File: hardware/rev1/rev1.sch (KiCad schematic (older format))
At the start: 37 parts, among them J1 Conn_01x09_Female, J2 RFM9X_header, J3 Conn_01x03_Male, U1 BNO055, U2 MPL3115A2, U3 Teensy3.6, U4 BMI088, U5 ADXL345BCCZ, Y1 Crystal_32kHz768

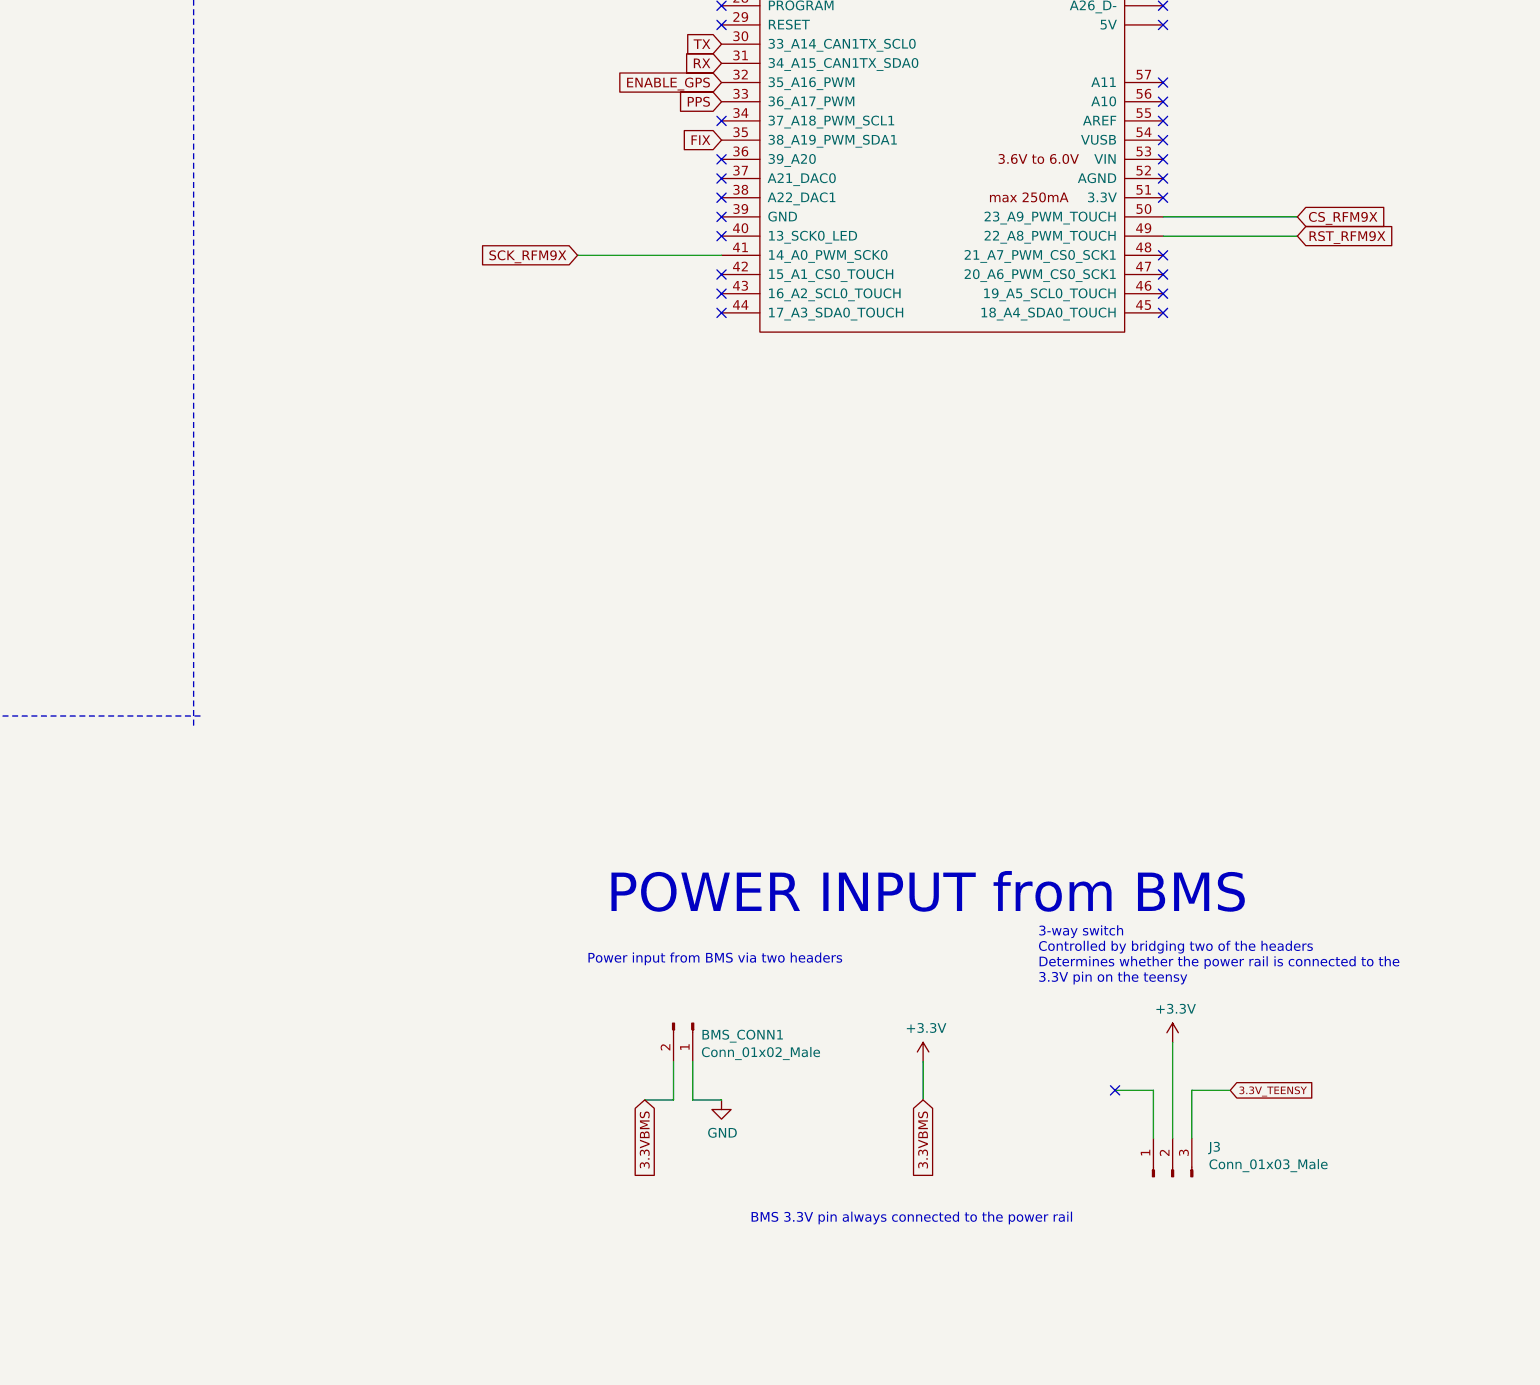
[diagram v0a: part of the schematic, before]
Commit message: add diode between Vin on Teensy and VDD on BMS
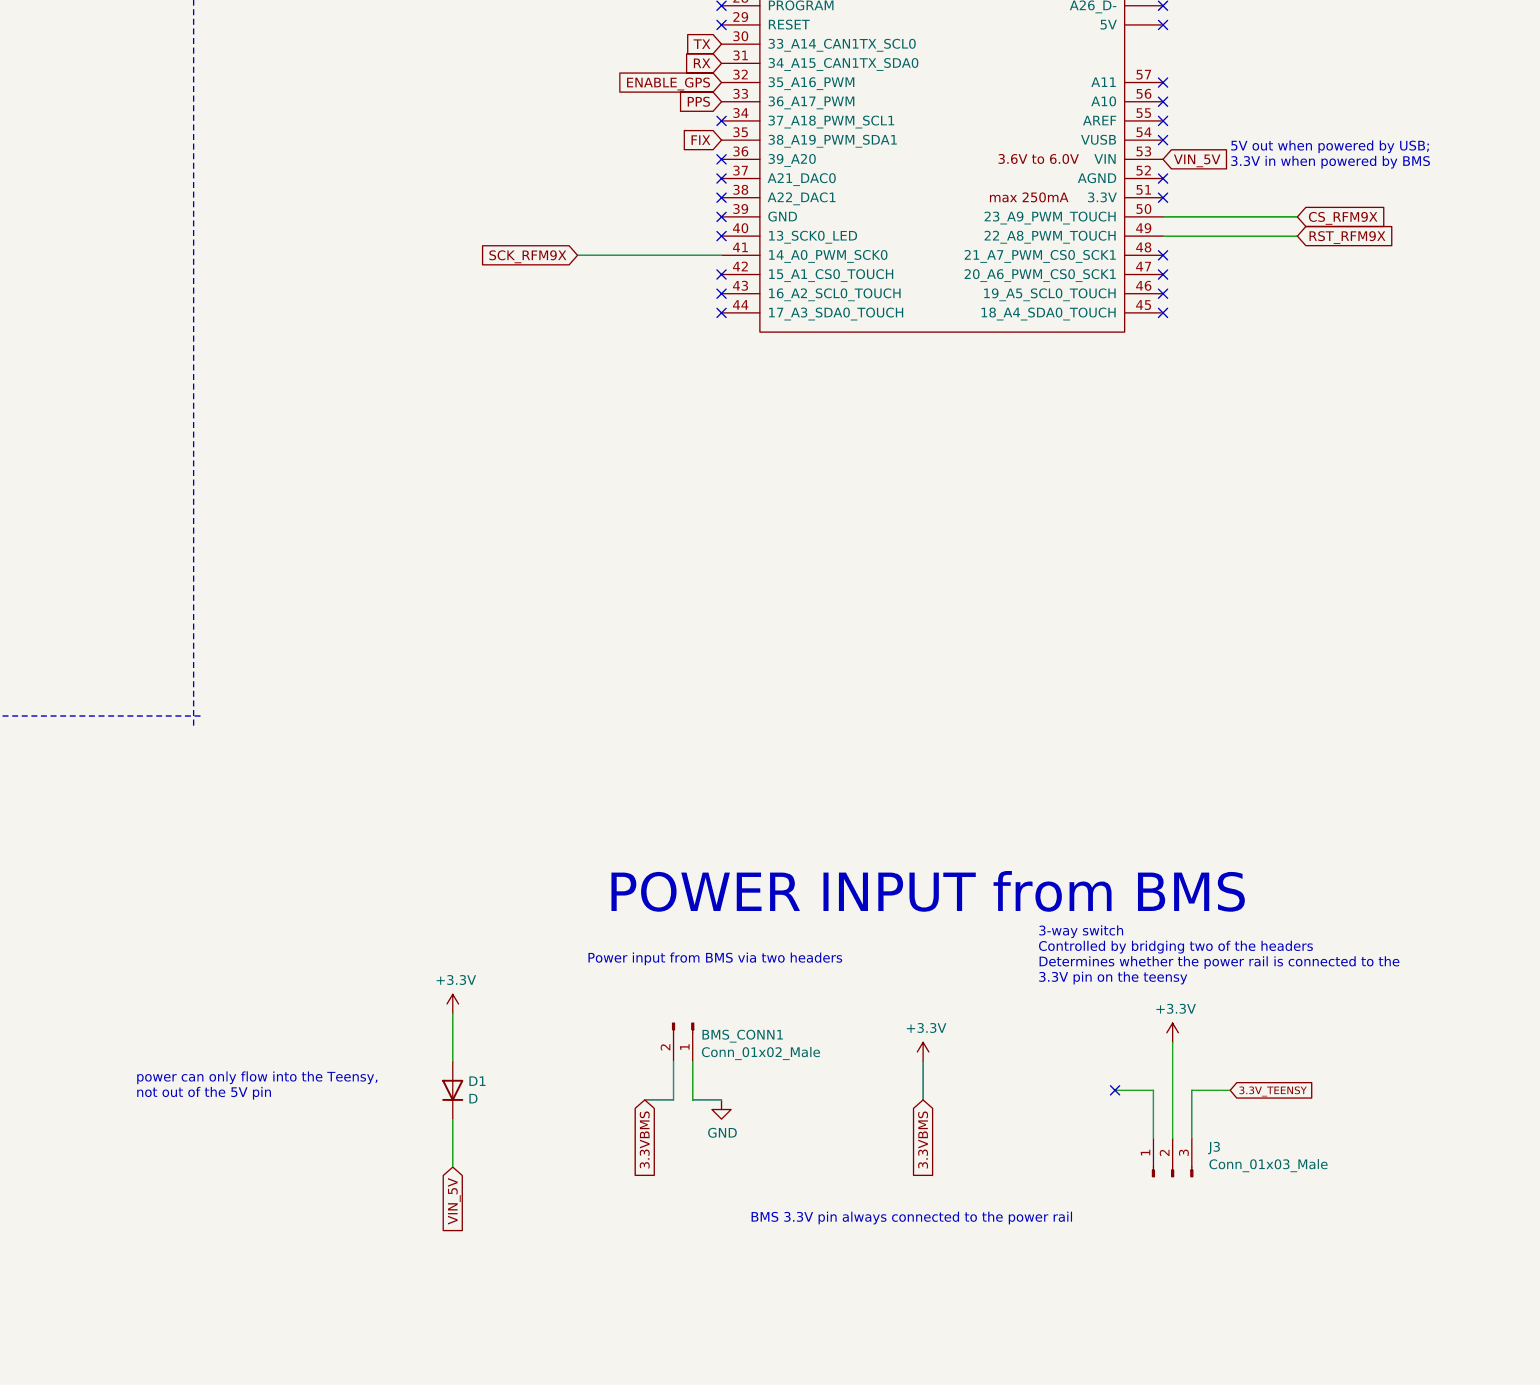
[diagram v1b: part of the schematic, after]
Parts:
- added D1: D, footprints:D_0805_OEM, symbol Device:D
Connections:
- net +3V3: now also D1.2 (A)
- net VIN_5V: now reaches U3.53 (VIN)
- net VIN_5V: now also D1.1 (K)
- no-connect marks 67 -> 66
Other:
- note added: "5V out when powered by USB;\n3.3V in when powered by BMS"
- note added: "power can only flow into the Teensy,\nnot out of the 5V pin"
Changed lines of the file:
@@
 Wire Wire Line
 	27250 11200 27400 11200
-NoConn ~ 29700 6300
 NoConn ~ 27400 4300
 NoConn ~ 27400 4400
@@
 NoConn ~ 29450 11150
 $Comp
-L power:GND #PWR?
+L power:GND #PWR04
 U 1 1 60246ABA
 P 27400 11200
-F 0 "#PWR?" H 27400 10950 50  0001 C CNN
+F 0 "#PWR04" H 27400 10950 50  0001 C CNN
 F 1 "GND" H 27405 11027 50  0000 C CNN
 F 2 "" H 27400 11200 50  0001 C CNN
@@
 	1    0    0    -1
 $EndComp
+Text GLabel 29700 6300 2    50   Input ~ 0
+VIN_5V
+Text Notes 30050 6350 0    50   ~ 0
+5V out when powered by USB;\n3.3V in when powered by BMS
+Text GLabel 26000 11550 3    50   Input ~ 0
+VIN_5V
+$Comp
+L power:+3.3V #PWR03
+U 1 1 6027438B
+P 26000 10750
+F 0 "#PWR03" H 26000 10600 50  0001 C CNN
+F 1 "+3.3V" H 26015 10923 50  0000 C CNN
+F 2 "" H 26000 10750 50  0001 C CNN
+F 3 "" H 26000 10750 50  0001 C CNN
+	1    26000 10750
+	1    0    0    -1
+$EndComp
+$Comp
+L Device:D D1
+U 1 1 60275618
+P 26000 11150
+F 0 "D1" V 26046 11070 50  0000 R CNN
+F 1 "D" V 25955 11070 50  0000 R CNN
+F 2 "footprints:D_0805_OEM" H 26000 11150 50  0001 C CNN
+F 3 "~" H 26000 11150 50  0001 C CNN
+	1    26000 11150
+	0    -1   -1   0
+$EndComp
+Wire Wire Line
+	26000 10750 26000 11000
+Wire Wire Line
+	26000 11300 26000 11550
+Text Notes 24350 11200 0    50   ~ 0
+power can only flow into the Teensy,\nnot out of the 5V pin
 $EndSCHEMATC

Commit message: move GPS pins away from Teensy
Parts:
- J3: footprint Connector_PinSocket_2.54mm:PinSocket_1x03_P2.54mm_Vertical -> Connector_PinHeader_2.54mm:PinHeader_1x03_P2.54mm_Vertical
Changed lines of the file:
@@
 F 0 "J3" V 29904 11412 50  0000 R CNN
 F 1 "Conn_01x03_Male" V 29813 11412 50  0000 R CNN
-F 2 "Connector_PinSocket_2.54mm:PinSocket_1x03_P2.54mm_Vertical" H 29750 11600 50  0001 C CNN
+F 2 "Connector_PinHeader_2.54mm:PinHeader_1x03_P2.54mm_Vertical" H 29750 11600 50  0001 C CNN
 F 3 "~" H 29750 11600 50  0001 C CNN
 	1    29750 11600

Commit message: modify circuit for power input from BMS on schematic
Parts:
- removed BMS_CONN1: Conn_01x02_Male, Connector_PinHeader_2.54mm:PinHeader_1x02_P2.54mm_Vertical, symbol Connector:Conn_01x02_Male
- added BMS_CONN2: Conn_01x04_Male, Connector_PinHeader_2.54mm:PinHeader_1x04_P2.54mm_Vertical, symbol Connector:Conn_01x04_Male
- added D? (x2): D, footprints:D_0805_OEM, symbol Device:D
- added Q?: Q_PNP_BCE, symbol Device:Q_PNP_BCE
- added R?: R_1.07K, footprints:R_0805_OEM, symbol preferred_parts:R_1.07K
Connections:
- net +3V3: now also D?.1 (K), D?.1 (K); no longer D1.2 (A), J1.7 (Pin_7), J1.9 (Pin_9)
- net GND: now also BMS_CONN2.1 (Pin_1)
- net RX: now also U3.30 (33_A14_CAN1TX_SCL0); no longer U3.31 (34_A15_CAN1TX_SDA0)
- net TX: now also U3.31 (34_A15_CAN1TX_SDA0); no longer U3.30 (33_A14_CAN1TX_SCL0)
- net VIN_5V renamed BMS_to_Teensy
- new net: BMS_CONN2.4 (Pin_4), D1.2 (A)
- new net: Q?.1 (B), R?.1
- new net: D?.2 (A), Q?.2 (C)
- new net BMS_to_sensors: BMS_CONN2.2 (Pin_2), D?.2 (A), R?.2
- new net BMS_to_sensors_backup: BMS_CONN2.3 (Pin_3), Q?.3 (E)
- no-connect marks 66 -> 68
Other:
- note added: "(GPS) RX -> TX (Teensy)\n(GPS) TX -> RX (Teensy)\n"
- note added: "TX\n\nRX"
- note removed: "BMS 3.3V pin always connected to the power rail"
- note removed: "Power input from BMS via two headers"
- moved on the sheet: D1
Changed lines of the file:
@@
-$EndComp
-$Comp
-L power:VDD #PWR0105
-U 1 1 5FED364A
-P 3750 8250
-F 0 "#PWR0105" H 3750 8100 50  0001 C CNN
-F 1 "VDD" H 3765 8423 50  0000 C CNN
-F 2 "" H 3750 8250 50  0001 C CNN
-F 3 "" H 3750 8250 50  0001 C CNN
-	1    3750 8250
-	1    0    0    -1
 $EndComp
 $Comp
@@
 Wire Wire Line
 	4150 4700 4150 5450
-$Comp
-L power:VDD #PWR0102
-U 1 1 5F89C575
-P 3500 2350
-F 0 "#PWR0102" H 3500 2200 50  0001 C CNN
-F 1 "VDD" H 3515 2523 50  0000 C CNN
-F 2 "" H 3500 2350 50  0001 C CNN
-F 3 "" H 3500 2350 50  0001 C CNN
-	1    3500 2350
-	1    0    0    -1
-$EndComp
 Connection ~ 5250 6950
 Wire Wire Line
@@
 	7250 7300 10200 7300
 $Comp
-L Connector:Conn_01x02_Male BMS_CONN1
-U 1 1 60257B5B
-P 27250 10800
-F 0 "BMS_CONN1" V 27312 10844 50  0000 L CNN
-F 1 "Conn_01x02_Male" V 27403 10844 50  0000 L CNN
-F 2 "Connector_PinHeader_2.54mm:PinHeader_1x02_P2.54mm_Vertical" H 27250 10800 50  0001 C CNN
-F 3 "~" H 27250 10800 50  0001 C CNN
-	1    27250 10800
-	0    1    1    0
-$EndComp
-$Comp
 L power:+3.3V #PWR0103
 U 1 1 60279C5C
@@
 	1    0    0    -1
 $EndComp
-Wire Wire Line
-	27000 11200 27150 11200
-Wire Wire Line
-	27150 11200 27150 11000
-Wire Wire Line
-	27250 11000 27250 11200
-Wire Wire Line
-	27250 11200 27400 11200
 NoConn ~ 27400 4300
 NoConn ~ 27400 4400
@@
 Text Notes 26800 10250 0    200  ~ 0
 POWER INPUT from BMS
-Connection ~ 18400 15200
-Wire Wire Line
-	18400 15900 18400 15400
-Wire Wire Line
-	18400 15200 18400 15050
 Text Notes 17850 14500 0    200  ~ 0
 GPS
@@
 Text GLabel 17800 15500 2    50   Input ~ 0
 FIX
-Text GLabel 17800 15400 2    50   Input ~ 0
-V_BACKUP
 Text GLabel 17800 15300 2    50   Input ~ 0
 ENABLE_GPS
-Wire Wire Line
-	17800 15200 18400 15200
 $Comp
 L preferred_parts:C_0.1uF C10
@@
 Text GLabel 27400 4600 0    50   Input ~ 0
 A0_ACCEL_BMI088
+Text GLabel 27400 5700 0    50   Input ~ 0
+RX
 Text GLabel 27400 5800 0    50   Input ~ 0
-RX
-Text GLabel 27400 5700 0    50   Input ~ 0
 TX
 Text GLabel 27400 6200 0    50   Input ~ 0
@@
 Text GLabel 27400 5900 0    50   Input ~ 0
 ENABLE_GPS
-Text GLabel 18650 15400 2    50   Input ~ 0
-V_BACKUP
-Wire Wire Line
-	18650 15400 18400 15400
-Connection ~ 18400 15400
-Wire Wire Line
-	18400 15400 18400 15200
 NoConn ~ 29700 3400
 NoConn ~ 29700 3300
@@
 Wire Wire Line
 	3500 2350 3500 3500
-Wire Wire Line
-	3300 8400 3750 8400
-Wire Wire Line
-	3750 8250 3750 8400
-Connection ~ 3750 8400
-Wire Wire Line
-	3750 8400 4200 8400
 $Comp
 L power:+3.3V #PWR0115
@@
 Text GLabel 30050 11150 2    39   Input ~ 0
 3.3V_TEENSY
-Text GLabel 27000 11200 3    50   Input ~ 0
-3.3VBMS
-$Comp
-L power:+3.3V #PWR0116
-U 1 1 601CF88A
-P 28450 11000
-F 0 "#PWR0116" H 28450 10850 50  0001 C CNN
-F 1 "+3.3V" H 28465 11173 50  0000 C CNN
-F 2 "" H 28450 11000 50  0001 C CNN
-F 3 "" H 28450 11000 50  0001 C CNN
-	1    28450 11000
-	1    0    0    -1
-$EndComp
-Text GLabel 28450 11200 3    50   Input ~ 0
-3.3VBMS
-Wire Wire Line
-	28450 11200 28450 11000
-Text Notes 27550 11850 0    50   ~ 0
-BMS 3.3V pin always connected to the power rail
-Text Notes 26700 10500 0    50   ~ 0
-Power input from BMS via two headers
 NoConn ~ 29450 11150
-$Comp
-L power:GND #PWR04
-U 1 1 60246ABA
-P 27400 11200
-F 0 "#PWR04" H 27400 10950 50  0001 C CNN
-F 1 "GND" H 27405 11027 50  0000 C CNN
-F 2 "" H 27400 11200 50  0001 C CNN
-F 3 "" H 27400 11200 50  0001 C CNN
-	1    27400 11200
-	1    0    0    -1
-$EndComp
-Text GLabel 29700 6300 2    50   Input ~ 0
-VIN_5V
-Text Notes 30050 6350 0    50   ~ 0
-5V out when powered by USB;\n3.3V in when powered by BMS
-Text GLabel 26000 11550 3    50   Input ~ 0
-VIN_5V
-$Comp
-L power:+3.3V #PWR03
-U 1 1 6027438B
-P 26000 10750
-F 0 "#PWR03" H 26000 10600 50  0001 C CNN
-F 1 "+3.3V" H 26015 10923 50  0000 C CNN
-F 2 "" H 26000 10750 50  0001 C CNN
-F 3 "" H 26000 10750 50  0001 C CNN
-	1    26000 10750
-	1    0    0    -1
-$EndComp
 $Comp
 L Device:D D1
 U 1 1 60275618
-P 26000 11150
-F 0 "D1" V 26046 11070 50  0000 R CNN
-F 1 "D" V 25955 11070 50  0000 R CNN
-F 2 "footprints:D_0805_OEM" H 26000 11150 50  0001 C CNN
-F 3 "~" H 26000 11150 50  0001 C CNN
-	1    26000 11150
+P 24650 11450
+F 0 "D1" V 24696 11370 50  0000 R CNN
+F 1 "D" V 24605 11370 50  0000 R CNN
+F 2 "footprints:D_0805_OEM" H 24650 11450 50  0001 C CNN
+F 3 "~" H 24650 11450 50  0001 C CNN
+	1    24650 11450
 	0    -1   -1   0
 $EndComp
-Wire Wire Line
-	26000 10750 26000 11000
-Wire Wire Line
-	26000 11300 26000 11550
-Text Notes 24350 11200 0    50   ~ 0
+Text Notes 23000 12100 0    50   ~ 0
 power can only flow into the Teensy,\nnot out of the 5V pin
+NoConn ~ 17800 15400
+Wire Wire Line
+	18400 15050 18400 15900
+NoConn ~ 17800 15200
+Text Notes 28500 5850 0    50   ~ 0
+TX\n\nRX
+$Comp
+L Connector:Conn_01x04_Male BMS_CONN2
+U 1 1 602BDAB1
+P 25200 10650
+F 0 "BMS_CONN2" V 25262 10794 50  0000 L CNN
+F 1 "Conn_01x04_Male" V 25353 10794 50  0000 L CNN
+F 2 "Connector_PinHeader_2.54mm:PinHeader_1x04_P2.54mm_Vertical" H 25200 10650 50  0001 C CNN
+F 3 "~" H 25200 10650 50  0001 C CNN
+	1    25200 10650
+	0    1    1    0
+$EndComp
+$Comp
+L power:GND #PWR?
+U 1 1 602C00BA
+P 25650 11350
+F 0 "#PWR?" H 25650 11100 50  0001 C CNN
+F 1 "GND" H 25655 11177 50  0000 C CNN
+F 2 "" H 25650 11350 50  0001 C CNN
+F 3 "" H 25650 11350 50  0001 C CNN
+	1    25650 11350
+	1    0    0    -1
+$EndComp
+Text GLabel 24650 11850 3    50   Input ~ 0
+BMS_to_Teensy
+Wire Wire Line
+	25200 10850 25200 11000
+Wire Wire Line
+	25100 10850 25100 11000
+Text GLabel 25100 11000 3    50   Input ~ 0
+BMS_to_sensors_backup
+Text GLabel 25200 11000 3    50   Input ~ 0
+BMS_to_sensors
+Text Notes 25800 5800 0    50   ~ 0
+(GPS) RX -> TX (Teensy)\n(GPS) TX -> RX (Teensy)\n
+Text Notes 30400 6350 0    50   ~ 0
+5V out when powered by USB;\n3.3V in when powered by BMS
+Text GLabel 29700 6300 2    50   Input ~ 0
+BMS_to_Teensy
+Wire Wire Line
+	24650 11850 24650 11600
+Wire Wire Line
+	25000 11200 24650 11200
+Wire Wire Line
+	24650 11200 24650 11300
+Wire Wire Line
+	25000 10850 25000 11200
+Wire Wire Line
+	25300 10850 25300 11200
+Wire Wire Line
+	25300 11200 25650 11200
+Wire Wire Line
+	25650 11350 25650 11200
+$Comp
+L Device:Q_PNP_BCE Q?
+U 1 1 60396DCD
+P 28050 12150
+F 0 "Q?" H 28240 12104 50  0000 L CNN
+F 1 "Q_PNP_BCE" H 28240 12195 50  0000 L CNN
+F 2 "" H 28250 12250 50  0001 C CNN
+F 3 "~" H 28050 12150 50  0001 C CNN
+	1    28050 12150
+	1    0    0    1
+$EndComp
+$Comp
+L Device:D D?
+U 1 1 60398902
+P 27150 12500
+F 0 "D?" V 27196 12420 50  0000 R CNN
+F 1 "D" V 27105 12420 50  0000 R CNN
+F 2 "footprints:D_0805_OEM" H 27150 12500 50  0001 C CNN
+F 3 "~" H 27150 12500 50  0001 C CNN
+	1    27150 12500
+	0    -1   -1   0
+$EndComp
+Wire Wire Line
+	28150 11500 28150 11950
+$Comp
+L preferred_parts:R_1.07K R?
+U 1 1 603A35C2
+P 27500 12150
+F 0 "R?" V 27293 12150 50  0000 C CNN
+F 1 "R_1.07K" V 27384 12150 50  0000 C CNN
+F 2 "footprints:R_0805_OEM" H 27430 12150 50  0001 C CNN
+F 3 "https://industrial.panasonic.com/cdbs/www-data/pdf/RDM0000/AOA0000C307.pdf" H 27580 12150 50  0001 C CNN
+F 4 "DK" H 27500 12150 60  0001 C CNN "MFN"
+F 5 "P1.07KDACT-ND" H 27500 12150 60  0001 C CNN "MPN"
+F 6 "https://www.digikey.com/product-detail/en/panasonic-electronic-components/ERA-6AEB1071V/P1.07KDACT-ND/3074919" H 27980 12550 60  0001 C CNN "PurchasingLink"
+	1    27500 12150
+	0    1    1    0
+$EndComp
+Wire Wire Line
+	27150 11500 27150 12150
+Wire Wire Line
+	27150 12150 27350 12150
+Wire Wire Line
+	27150 12150 27150 12350
+Connection ~ 27150 12150
+Wire Wire Line
+	27650 12150 27850 12150
+Wire Wire Line
+	28150 12350 28150 12850
+Wire Wire Line
+	27150 13250 26700 13250
+Wire Wire Line
+	26700 13250 26700 13150
+$Comp
+L power:+3.3V #PWR?
+U 1 1 603D4A0D
+P 26700 13150
+F 0 "#PWR?" H 26700 13000 50  0001 C CNN
+F 1 "+3.3V" H 26715 13323 50  0000 C CNN
+F 2 "" H 26700 13150 50  0001 C CNN
+F 3 "" H 26700 13150 50  0001 C CNN
+	1    26700 13150
+	1    0    0    -1
+$EndComp
+Text GLabel 27150 11500 1    50   Input ~ 0
+BMS_to_sensors
+Text GLabel 28150 11500 1    50   Input ~ 0
+BMS_to_sensors_backup
+$Comp
+L Device:D D?
+U 1 1 603EDD6A
+P 27650 12850
+F 0 "D?" V 27696 12770 50  0000 R CNN
+F 1 "D" V 27605 12770 50  0000 R CNN
+F 2 "footprints:D_0805_OEM" H 27650 12850 50  0001 C CNN
+F 3 "~" H 27650 12850 50  0001 C CNN
+	1    27650 12850
+	1    0    0    -1
+$EndComp
+Wire Wire Line
+	27150 12650 27150 12850
+Wire Wire Line
+	28150 12850 27800 12850
+Wire Wire Line
+	27500 12850 27150 12850
+Connection ~ 27150 12850
+Wire Wire Line
+	27150 12850 27150 13250
+Wire Wire Line
+	3300 8400 4200 8400
+$Comp
+L power:+3.3V #PWR?
+U 1 1 6045910E
+P 3500 2350
+F 0 "#PWR?" H 3500 2200 50  0001 C CNN
+F 1 "+3.3V" H 3515 2523 50  0000 C CNN
+F 2 "" H 3500 2350 50  0001 C CNN
+F 3 "" H 3500 2350 50  0001 C CNN
+	1    3500 2350
+	1    0    0    -1
+$EndComp
 $EndSCHEMATC
